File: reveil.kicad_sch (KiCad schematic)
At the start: 15 parts, among them J1 Barrel_Jack_Switch, J2 AudioJack3, M1 Motor_DC, Q1 2N3904, Q2 IRF540N, SW1 SW_SPDT

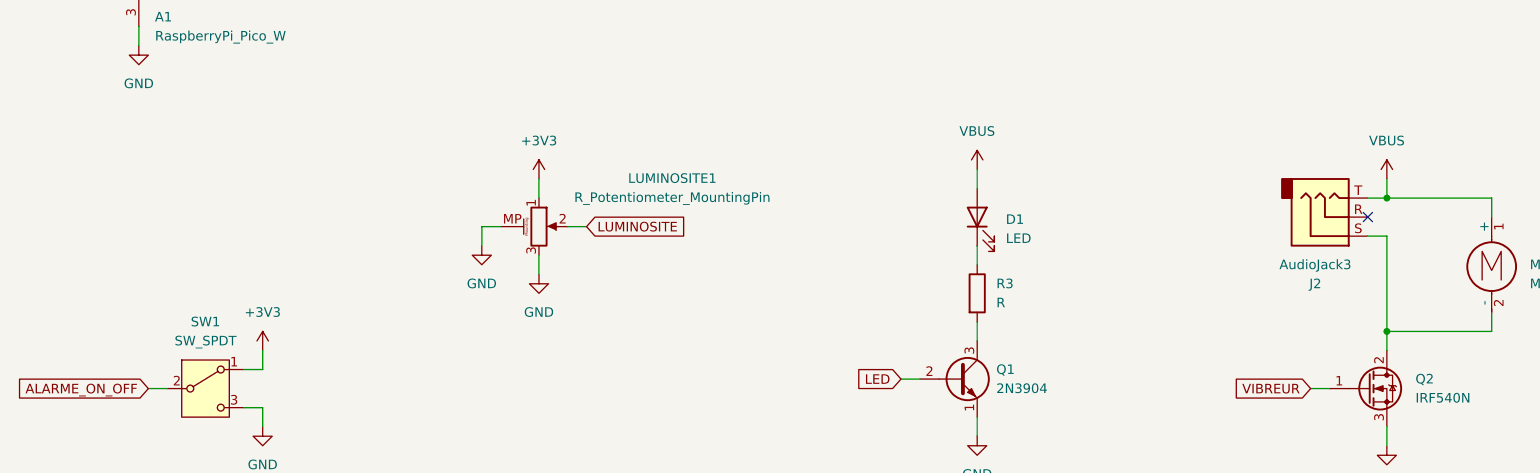
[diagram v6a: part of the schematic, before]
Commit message: all footprints and placements
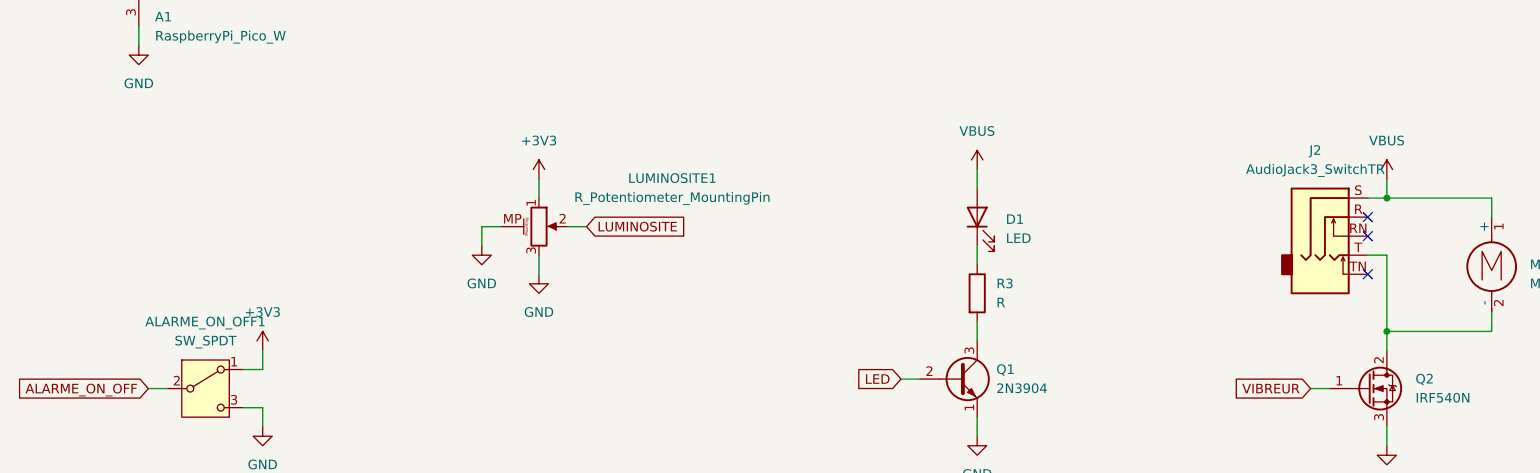
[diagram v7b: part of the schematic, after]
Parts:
- removed J2: AudioJack3, symbol Connector_Audio:AudioJack3
- added J2: AudioJack3_SwitchTR, Connector_Audio:Jack_3.5mm_CUI_SJ1-3525N_Horizontal, symbol Connector_Audio:AudioJack3_SwitchTR
- A1: footprint Module:RaspberryPi_Pico_W_SMD_HandSolder -> Module:RaspberryPi_Pico_Common_THT
- renumbered SW1 to ALARME_ON_OFF1
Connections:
- net VBUS: now also J2.S
- net at M1.2 (-), Q2.2 (D): now also J2.T
- no-connect marks 11 -> 13
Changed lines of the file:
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@@
 	)
 	(no_connect
+		(at 246.38 124.46)
+	)
+	(no_connect
+		(at 246.38 129.54)
+	)
+	(no_connect
+		(at 246.38 121.92)
+	)
+	(no_connect
 		(at 105.41 76.2)
 	)
@@
 	)
 	(no_connect
-		(at 246.38 121.92)
-	)
-	(no_connect
 		(at 105.41 60.96)
 	)
@@
 	(wire
 		(pts
-			(xy 248.92 124.46) (xy 246.38 124.46)
-		)
-		(stroke
-			(width 0)
-			(type default)
-		)
-	)
-	(wire
-		(pts
 			(xy 165.1 35.56) (xy 170.18 35.56)
 		)
@@
 	(wire
 		(pts
-			(xy 248.92 124.46) (xy 248.92 137.16)
-		)
-		(stroke
-			(width 0)
-			(type default)
-		)
-	)
-	(wire
-		(pts
 			(xy 57.15 78.74) (xy 59.69 78.74)
 		)
@@
 	(wire
 		(pts
+			(xy 246.38 127) (xy 248.92 127)
+		)
+		(stroke
+			(width 0)
+			(type default)
+		)
+	)
+	(wire
+		(pts
 			(xy 262.89 134.62) (xy 262.89 137.16)
 		)
@@
 	(wire
 		(pts
+			(xy 248.92 127) (xy 248.92 137.16)
+		)
+		(stroke
+			(width 0)
+			(type default)
+		)
+	)
+	(wire
+		(pts
 			(xy 194.31 151.13) (xy 194.31 148.59)
 		)
@@
 		(dnp no)
 		(fields_autoplaced yes)
-		(property "Reference" "SW1"
+		(property "Reference" "ALARME_ON_OFF1"
 			(at 91.44 135.89 0)
 			(effects
@@
 			(project ""
 				(path "/6015885c-867c-4e88-9a3e-de8167bfed74"
-					(reference "SW1")
+					(reference "ALARME_ON_OFF1")
 					(unit 1)
 				)
@@
 	)
 	(symbol
+		(lib_id "Connector_Audio:AudioJack3_SwitchTR")
+		(at 241.3 121.92 0)
+		(unit 1)
+		(exclude_from_sim no)
+		(in_bom yes)
+		(on_board yes)
+		(dnp no)
+		(fields_autoplaced yes)
+		(property "Reference" "J2"
+			(at 239.395 113.03 0)
+			(effects
+				(font
+					(size 1.27 1.27)
+				)
+			)
+		)
+		(property "Value" "AudioJack3_SwitchTR"
+			(at 239.395 115.57 0)
+			(effects
+				(font
+					(size 1.27 1.27)
+				)
+			)
+		)
+		(property "Footprint" "Connector_Audio:Jack_3.5mm_CUI_SJ1-3525N_Horizontal"
+			(at 241.3 121.92 0)
+			(effects
+				(font
+					(size 1.27 1.27)
+				)
+				(hide yes)
+			)
+		)
+		(property "Datasheet" "~"
+			(at 241.3 121.92 0)
+			(effects
+				(font
+					(size 1.27 1.27)
+				)
+				(hide yes)
+			)
+		)
+		(property "Description" "Audio Jack, 3 Poles (Stereo / TRS), Switched TR Poles (Normalling)"
+			(at 241.3 121.92 0)
+			(effects
+				(font
+					(size 1.27 1.27)
+				)
+				(hide yes)
+			)
+		)
+		(pin "TN"
+		)
+		(pin "RN"
+		)
+		(pin "S"
+		)
+		(pin "R"
+		)
+		(pin "T"
+		)
+		(instances
+			(project ""
+				(path "/6015885c-867c-4e88-9a3e-de8167bfed74"
+					(reference "J2")
+					(unit 1)
+				)
+			)
+		)
+	)
+	(symbol
 		(lib_id "Graphic:Logo_Open_Hardware_Small")
 		(at 29.21 149.86 0)
@@
 	)
 	(symbol
-		(lib_id "Connector_Audio:AudioJack3")
-		(at 241.3 121.92 0)
-		(mirror x)
-		(unit 1)
-		(exclude_from_sim no)
-		(in_bom yes)
-		(on_board yes)
-		(dnp no)
-		(property "Reference" "J2"
-			(at 239.395 130.81 0)
-			(effects
-				(font
-					(size 1.27 1.27)
-				)
-			)
-		)
-		(property "Value" "AudioJack3"
-			(at 239.395 128.27 0)
-			(effects
-				(font
-					(size 1.27 1.27)
-				)
-			)
-		)
-		(property "Footprint" ""
-			(at 241.3 121.92 0)
-			(effects
-				(font
-					(size 1.27 1.27)
-				)
-				(hide yes)
-			)
-		)
-		(property "Datasheet" "~"
-			(at 241.3 121.92 0)
-			(effects
-				(font
-					(size 1.27 1.27)
-				)
-				(hide yes)
-			)
-		)
-		(property "Description" "Audio Jack, 3 Poles (Stereo / TRS)"
-			(at 241.3 121.92 0)
-			(effects
-				(font
-					(size 1.27 1.27)
-				)
-				(hide yes)
-			)
-		)
-		(pin "T"
-		)
-		(pin "S"
-		)
-		(pin "R"
-		)
-		(instances
-			(project ""
-				(path "/6015885c-867c-4e88-9a3e-de8167bfed74"
-					(reference "J2")
-					(unit 1)
-				)
-			)
-		)
-	)
-	(symbol
 		(lib_id "power:VBUS")
 		(at 194.31 115.57 0)
@@
 			)
 		)
-		(property "Footprint" "Module:RaspberryPi_Pico_W_SMD_HandSolder"
+		(property "Footprint" "Module:RaspberryPi_Pico_Common_THT"
 			(at 82.55 107.95 0)
 			(effects

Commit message: routing completed
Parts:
- J1: footprint (none) -> Connector_BarrelJack:BarrelJack_Wuerth_6941xx301002
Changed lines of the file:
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@@
 			)
 		)
-		(property "Footprint" ""
+		(property "Footprint" "Connector_BarrelJack:BarrelJack_Wuerth_6941xx301002"
 			(at 36.83 121.666 0)
 			(effects
